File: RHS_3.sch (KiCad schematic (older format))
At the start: 64 parts, among them IC1 ATMEGA328P-A, IC2 CC1101, IC3 CC1101_Chip, J1 Glass Breakage Detector, J2 ANT, P4 ISP Bottom, P5 ISP Top, P6 FTDI, P7 ISP 10, SW1 Reset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

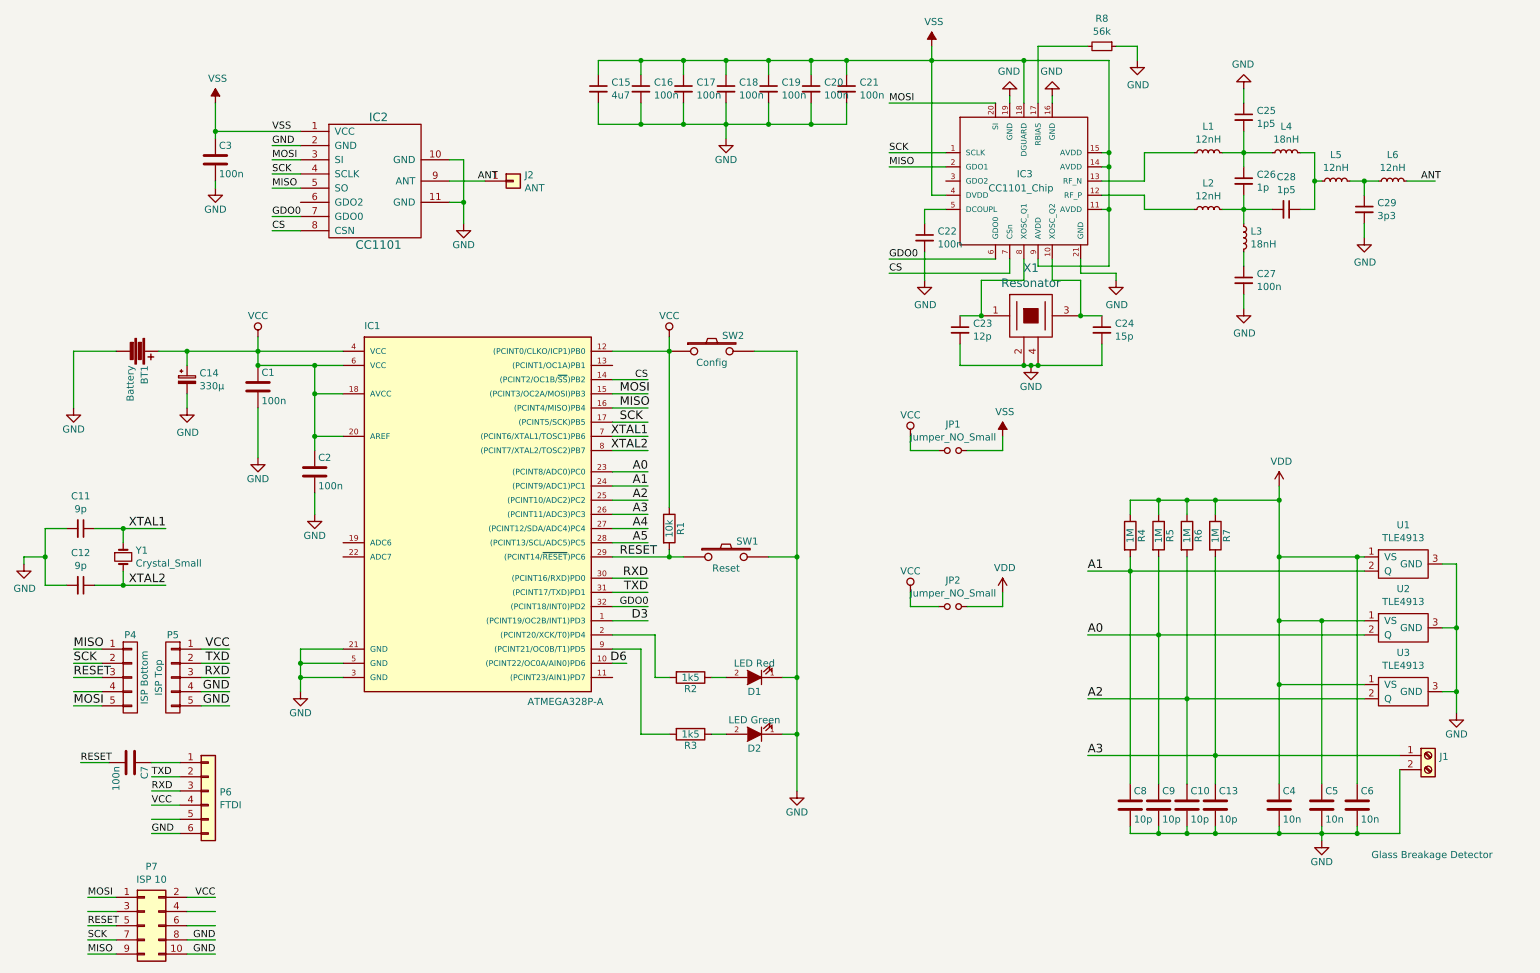
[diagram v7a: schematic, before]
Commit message: switches for TLEs & CC1101 added
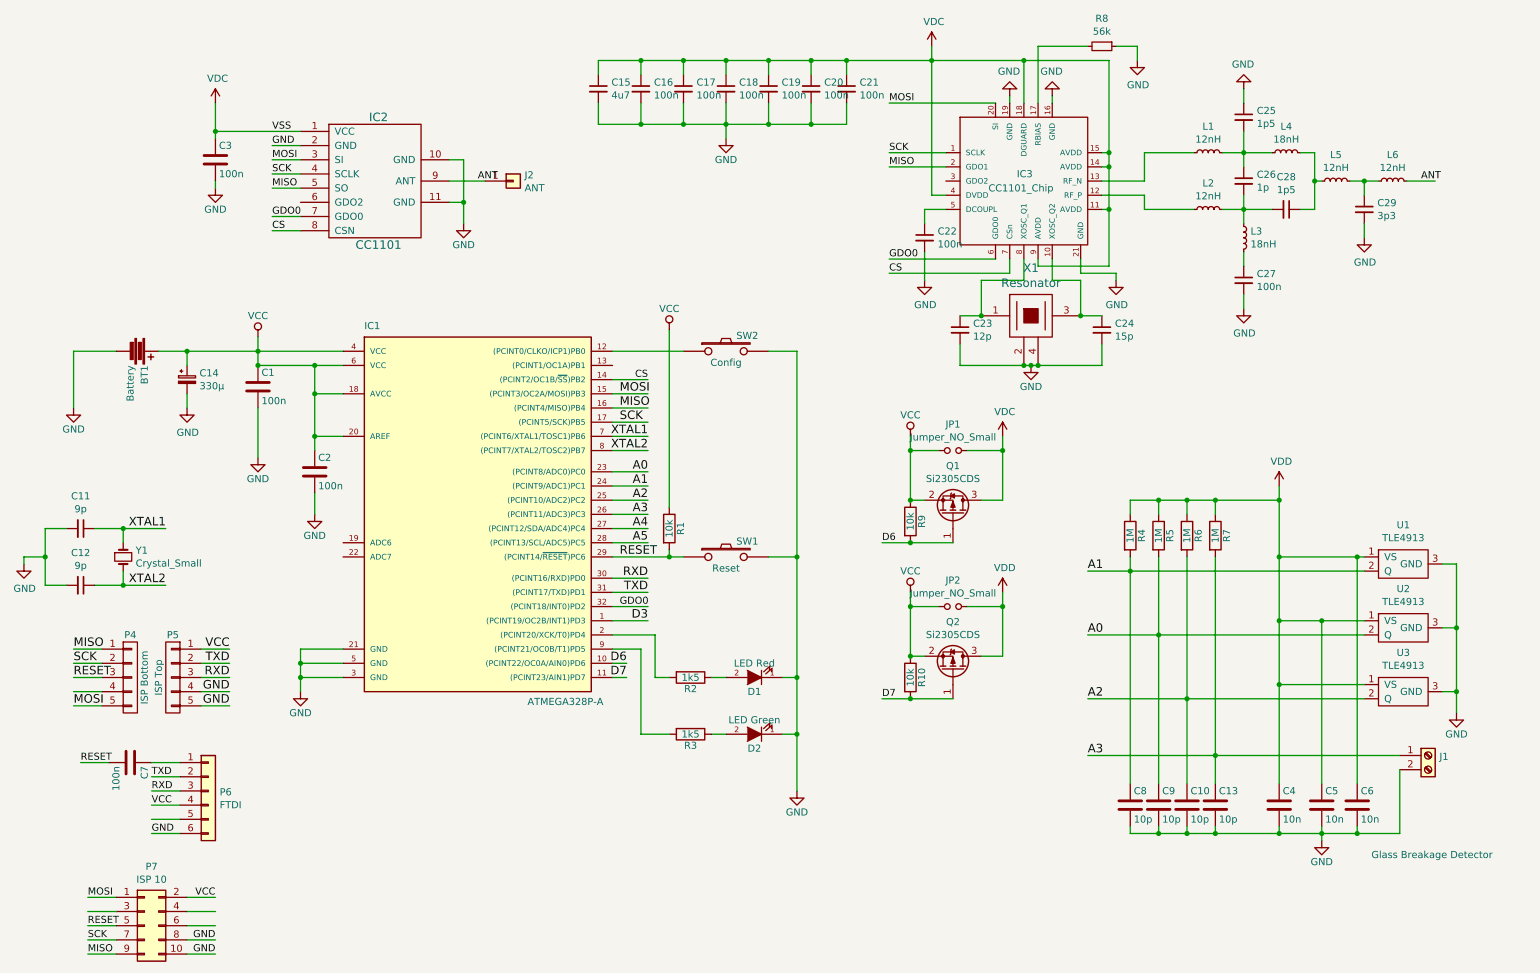
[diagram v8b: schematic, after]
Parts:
- added Q1, Q2: Si2305CDS, Package_TO_SOT_SMD:SOT-23, symbol Transistor_FET:Si2319CDS
- added R10, R9: 10k, Resistor_SMD:R_0805_2012Metric_Pad1.15x1.40mm_HandSolder, symbol RHS_3-rescue:R-RHS_2-rescue
- R8: LCSC Part # (none) -> C25796
- U1, U2, U3: LCSC Part # (none) -> C126654
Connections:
- net labels added: D7, VDC
- wire segments 285 -> 297
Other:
- moved on the sheet: SW2
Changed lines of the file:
@@
 L RHS_3-rescue:SW_PUSH-RHS_2-rescue SW2
 U 1 1 591051B2
-P 5650 2850
-F 0 "SW2" H 5800 2960 50  0000 C CNN
-F 1 "Config" H 5650 2770 50  0000 C CNN
-F 2 "libraries:MicroSwitch_3x4" H 5650 2850 50  0001 C CNN
-F 3 "" H 5650 2850 50  0000 C CNN
-	1    5650 2850
+P 5750 2850
+F 0 "SW2" H 5900 2960 50  0000 C CNN
+F 1 "Config" H 5750 2770 50  0000 C CNN
+F 2 "libraries:MicroSwitch_3x4" H 5750 2850 50  0001 C CNN
+F 3 "" H 5750 2850 50  0000 C CNN
+	1    5750 2850
 	1    0    0    -1
 $EndComp
@@
 	-1   0    0    -1
 $EndComp
-Wire Wire Line
-	4950 2850 5350 2850
-Wire Wire Line
-	5950 2850 6250 2850
 Wire Wire Line
 	6250 2850 6250 4300
@@
 F 2 "Package_TO_SOT_SMD:SOT-23" H 10550 4300 50  0001 C CNN
 F 3 "" H 10550 4300 50  0001 C CNN
+F 4 "C126654" H 10550 4300 50  0001 C CNN "LCSC Part #"
 	1    10550 4300
 	1    0    0    -1
@@
 F 2 "Package_TO_SOT_SMD:SOT-23" H 10550 4750 50  0001 C CNN
 F 3 "" H 10550 4750 50  0001 C CNN
+F 4 "C126654" H 10550 4750 50  0001 C CNN "LCSC Part #"
 	1    10550 4750
 	1    0    0    -1
@@
 F 2 "Package_TO_SOT_SMD:SOT-23" H 10550 5200 50  0001 C CNN
 F 3 "" H 10550 5200 50  0001 C CNN
+F 4 "C126654" H 10550 5200 50  0001 C CNN "LCSC Part #"
 	1    10550 5200
 	1    0    0    -1
@@
 Wire Wire Line
 	1950 2850 2450 2850
-Connection ~ 5350 2850
-Wire Wire Line
-	5350 2850 5350 3950
 $Comp
 L cc1101:CC1101_Chip IC3
@@
 L RHS_3-rescue:VCC-RHS_2-rescue #PWR0105
 U 1 1 5F909869
-P 5350 2750
-F 0 "#PWR0105" H 5350 2600 50  0001 C CNN
-F 1 "VCC" H 5350 2900 50  0000 C CNN
-F 2 "" H 5350 2750 50  0000 C CNN
-F 3 "" H 5350 2750 50  0000 C CNN
-	1    5350 2750
-	1    0    0    -1
-$EndComp
-Wire Wire Line
-	5350 2750 5350 2850
+P 5350 2700
+F 0 "#PWR0105" H 5350 2550 50  0001 C CNN
+F 1 "VCC" H 5350 2850 50  0000 C CNN
+F 2 "" H 5350 2700 50  0000 C CNN
+F 3 "" H 5350 2700 50  0000 C CNN
+	1    5350 2700
+	1    0    0    -1
+$EndComp
 Wire Wire Line
 	2150 1100 2150 1300
@@
 F 2 "Resistor_SMD:R_0402_1005Metric" H 8400 700 50  0001 C CNN
 F 3 "~" H 8400 700 50  0001 C CNN
+F 4 "C25796" H 8400 700 50  0001 C CNN "LCSC Part #"
 	1    8400 700
 	0    1    1    0
@@
 Wire Wire Line
 	5150 800  5450 800
-$Comp
-L power:VSS #PWR0110
-U 1 1 5F820753
-P 7200 700
-F 0 "#PWR0110" H 7200 550 50  0001 C CNN
-F 1 "VSS" H 7215 873 50  0000 C CNN
-F 2 "" H 7200 700 50  0001 C CNN
-F 3 "" H 7200 700 50  0001 C CNN
-	1    7200 700
-	1    0    0    -1
-$EndComp
 Wire Wire Line
 	7200 700  7200 800
-$Comp
-L power:VSS #PWR0117
-U 1 1 5F83527D
-P 2150 1100
-F 0 "#PWR0117" H 2150 950 50  0001 C CNN
-F 1 "VSS" H 2165 1273 50  0000 C CNN
-F 2 "" H 2150 1100 50  0001 C CNN
-F 3 "" H 2150 1100 50  0001 C CNN
-	1    2150 1100
-	1    0    0    -1
-$EndComp
-$Comp
-L power:VSS #PWR0118
-U 1 1 5F8358EE
-P 7700 3450
-F 0 "#PWR0118" H 7700 3300 50  0001 C CNN
-F 1 "VSS" H 7715 3623 50  0000 C CNN
-F 2 "" H 7700 3450 50  0001 C CNN
-F 3 "" H 7700 3450 50  0001 C CNN
-	1    7700 3450
-	1    0    0    -1
-$EndComp
 $Comp
 L RHS_3-rescue:VCC-RHS_2-rescue #PWR0119
@@
 	7700 3550 7700 3450
 $Comp
-L power:VDD #PWR?
+L power:VDD #PWR0121
 U 1 1 5F8640A1
 P 9650 3800
-F 0 "#PWR?" H 9650 3650 50  0001 C CNN
+F 0 "#PWR0121" H 9650 3650 50  0001 C CNN
 F 1 "VDD" H 9665 3973 50  0000 C CNN
 F 2 "" H 9650 3800 50  0001 C CNN
@@
 Wire Wire Line
 	7450 4650 7700 4650
+Wire Wire Line
+	5350 2700 5350 3950
+Wire Wire Line
+	4950 2850 5450 2850
+Wire Wire Line
+	6050 2850 6250 2850
+$Comp
+L power:VDC #PWR0110
+U 1 1 5F8B5E7B
+P 7700 3450
+F 0 "#PWR0110" H 7700 3350 50  0001 C CNN
+F 1 "VDC" H 7715 3623 50  0000 C CNN
+F 2 "" H 7700 3450 50  0001 C CNN
+F 3 "" H 7700 3450 50  0001 C CNN
+	1    7700 3450
+	1    0    0    -1
+$EndComp
+$Comp
+L power:VDC #PWR0118
+U 1 1 5F8B6796
+P 7200 700
+F 0 "#PWR0118" H 7200 600 50  0001 C CNN
+F 1 "VDC" H 7215 873 50  0000 C CNN
+F 2 "" H 7200 700 50  0001 C CNN
+F 3 "" H 7200 700 50  0001 C CNN
+	1    7200 700
+	1    0    0    -1
+$EndComp
+$Comp
+L Transistor_FET:Si2319CDS Q1
+U 1 1 5F8C85CD
+P 7350 4000
+F 0 "Q1" V 7692 4000 50  0000 C CNN
+F 1 "Si2305CDS" V 7601 4000 50  0000 C CNN
+F 2 "Package_TO_SOT_SMD:SOT-23" H 7550 3925 50  0001 L CIN
+F 3 "" H 7350 4000 50  0001 L CNN
+F 4 "C37577" H 7350 4000 50  0001 C CNN "LCSC Part #"
+	1    7350 4000
+	0    1    -1   0
+$EndComp
+Wire Wire Line
+	7150 3900 7050 3900
+Wire Wire Line
+	7050 3900 7050 3550
+Connection ~ 7050 3550
+Wire Wire Line
+	7550 3900 7700 3900
+Wire Wire Line
+	7700 3900 7700 3550
+Connection ~ 7700 3550
+$Comp
+L Transistor_FET:Si2319CDS Q2
+U 1 1 5F922FF9
+P 7350 5100
+F 0 "Q2" V 7692 5100 50  0000 C CNN
+F 1 "Si2305CDS" V 7601 5100 50  0000 C CNN
+F 2 "Package_TO_SOT_SMD:SOT-23" H 7550 5025 50  0001 L CIN
+F 3 "" H 7350 5100 50  0001 L CNN
+F 4 "C37577" H 7350 5100 50  0001 C CNN "LCSC Part #"
+	1    7350 5100
+	0    1    -1   0
+$EndComp
+Wire Wire Line
+	7050 4650 7050 5000
+Wire Wire Line
+	7050 5000 7150 5000
+Connection ~ 7050 4650
+Wire Wire Line
+	7550 5000 7700 5000
+Wire Wire Line
+	7700 5000 7700 4650
+Connection ~ 7700 4650
+Wire Wire Line
+	7350 5300 7050 5300
+Wire Wire Line
+	6850 4200 7050 4200
+$Comp
+L RHS_3-rescue:R-RHS_2-rescue R9
+U 1 1 5F9810D1
+P 7050 4050
+F 0 "R9" V 7130 4050 50  0000 C CNN
+F 1 "10k" V 7050 4050 50  0000 C CNN
+F 2 "Resistor_SMD:R_0805_2012Metric_Pad1.15x1.40mm_HandSolder" V 6980 4050 50  0001 C CNN
+F 3 "" H 7050 4050 50  0000 C CNN
+F 4 "C17414" H 7050 4050 50  0001 C CNN "LCSC Part #"
+	1    7050 4050
+	1    0    0    -1
+$EndComp
+Connection ~ 7050 3900
+Connection ~ 7050 4200
+Wire Wire Line
+	7050 4200 7350 4200
+$Comp
+L RHS_3-rescue:R-RHS_2-rescue R10
+U 1 1 5F98187C
+P 7050 5150
+F 0 "R10" V 7130 5150 50  0000 C CNN
+F 1 "10k" V 7050 5150 50  0000 C CNN
+F 2 "Resistor_SMD:R_0805_2012Metric_Pad1.15x1.40mm_HandSolder" V 6980 5150 50  0001 C CNN
+F 3 "" H 7050 5150 50  0000 C CNN
+F 4 "C17414" H 7050 5150 50  0001 C CNN "LCSC Part #"
+	1    7050 5150
+	1    0    0    -1
+$EndComp
+Connection ~ 7050 5000
+Connection ~ 7050 5300
+Wire Wire Line
+	7050 5300 6850 5300
+Wire Wire Line
+	4950 5150 5050 5150
+Text Label 5050 5150 2    60   ~ 0
+D7
+Text Label 6850 4200 0    50   ~ 0
+D6
+Text Label 6850 5300 0    50   ~ 0
+D7
+$Comp
+L power:VDC #PWR?
+U 1 1 5F9A9FD9
+P 2150 1100
+F 0 "#PWR?" H 2150 1000 50  0001 C CNN
+F 1 "VDC" H 2165 1273 50  0000 C CNN
+F 2 "" H 2150 1100 50  0001 C CNN
+F 3 "" H 2150 1100 50  0001 C CNN
+	1    2150 1100
+	1    0    0    -1
+$EndComp
 $EndSCHEMATC
